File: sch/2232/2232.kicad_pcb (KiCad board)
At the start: 2 copper layers, 80 x 70 mm, 65 parts, among them J1 47346-0001, J2 IDC-06, J3 IDC-06, J4 IDC-10, J5 IDC-10, J6 6P6C, J7 Screw_Terminal_01x06, J8 Screw_Terminal_01x06, U1 FT2232D, U2 AMS1117-3.3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

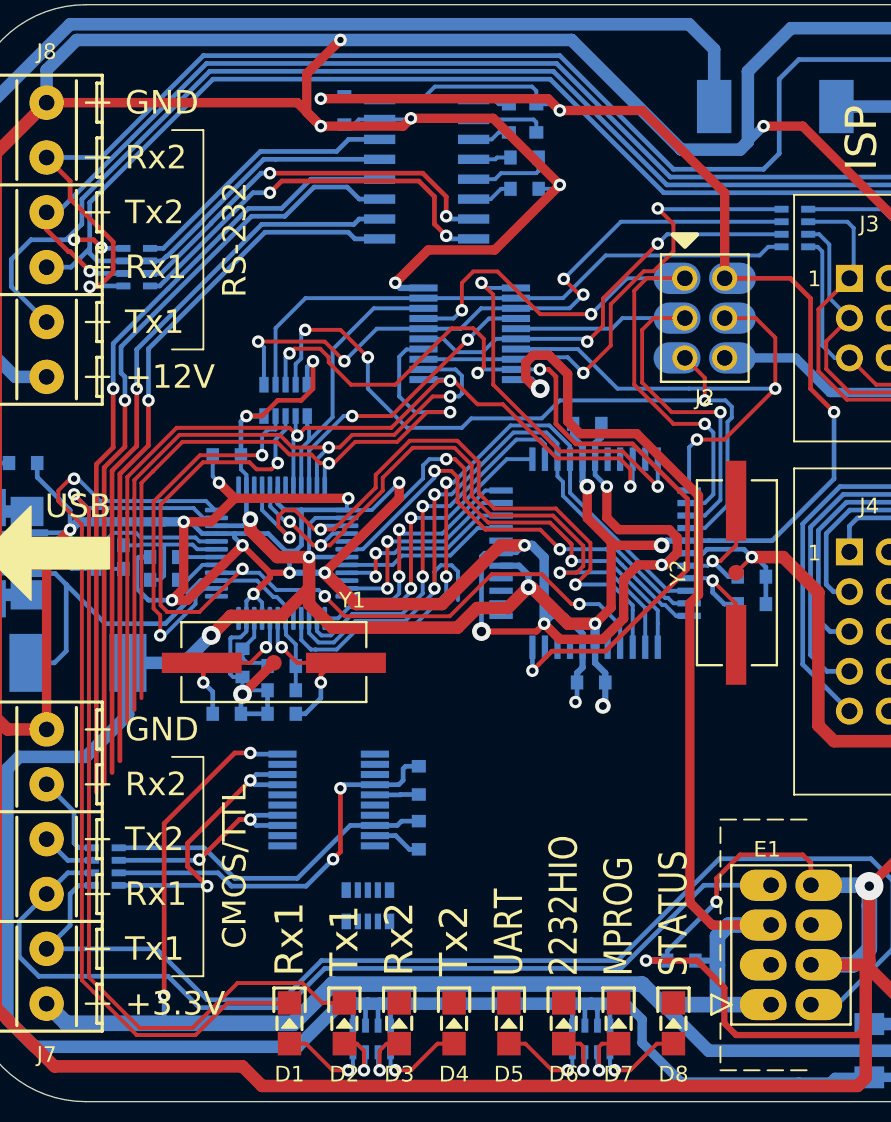
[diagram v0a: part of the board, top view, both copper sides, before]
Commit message: All footprinted elements are routed
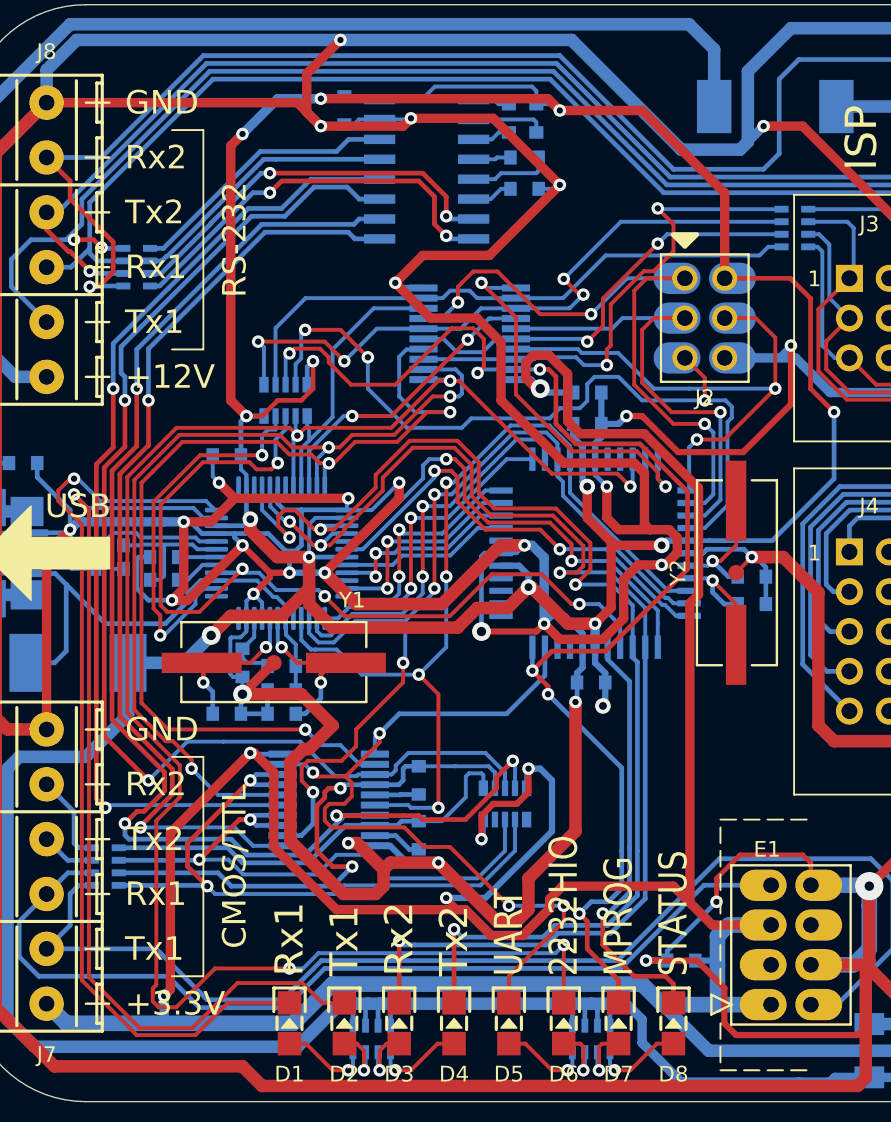
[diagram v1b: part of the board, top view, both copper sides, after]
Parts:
- added C21: 0.22u, NevaDA:C_0603, B.Cu at (99.5, 89.8)
- moved RN4 10.9 mm to (94.2, 116.0)
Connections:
- RN4 pad 1: /TX1_RS_3 -> /RX2_3V
- RN4 pad 2: /TX2_RS_3 -> /RX1_3V
- RN4 pad 3: /RX2_3V -> /TX1_RS_3
- RN4 pad 4: /RX1_3V -> /TX2_RS_3
- RN4 pad 6: /TX2_3V -> (no net)
- RN4 pad 8: (no net) -> /TX2_3V
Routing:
- net GNDD: track 725.4 -> 836.0 mm, vias 32 -> 36
- net +3V3: track 187.6 -> 251.6 mm, vias 3 -> 6
- net /EN_UART: track 0.00 -> 52.8 mm, vias 0 -> 4
- net /FBUFF: track 62.4 -> 113.4 mm, vias 3 -> 5
- net /TX2_RS_3: track 46.6 -> 88.4 mm, vias 1 -> 4
- net /LED3_~RD: track 42.9 -> 79.9 mm, vias 3 -> 4
- net /LED4_~WR: track 44.5 -> 78.2 mm, vias 3 -> 4
- net /TX1_RS_3: track 49.6 -> 77.5 mm, vias 1 -> 2
- net /MCU_LED: track 0.00 -> 27.2 mm, vias 0 -> 1
- net /MCU_BUFF: track 57.1 -> 83.8 mm, vias 4 -> 6
- net +5V: track 316.2 -> 340.9 mm, vias 13 -> 14
- net /TX2_3V: track 13.8 -> 37.6 mm
- net /TX1_3V: track 19.0 -> 42.0 mm
- net /FSCK_T1: track 46.1 -> 62.9 mm, vias 2 -> 3
- net /PAR_0_T2: track 42.6 -> 59.0 mm, vias 2 -> 4
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
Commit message: VCC routed
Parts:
- added D10: SMBJ5.0A-E3/52, NevaDA:DO-214AA_SMB, B.Cu at (126.5, 109.0)
- added Q1: BC817-40, NevaDA:SOT-23, B.Cu at (136.0, 95.0)
- added Q2: FZT1049A, NevaDA:SOT-223, B.Cu at (123.0, 93.5)
- added R11: 100, NevaDA:R_0603, B.Cu at (151.6, 78.9)
- added R12: 100, NevaDA:R_0603, B.Cu at (146.9, 78.5)
- added R13: 100, NevaDA:R_0603, B.Cu at (131.8, 94.0)
- added R8: 100, NevaDA:R_0603, B.Cu at (142.5, 78.5)
- added R9: 1 1206, NevaDA:R_1206, B.Cu at (137.0, 100.8)
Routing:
- net VCC: track 32.1 -> 196.0 mm, vias 0 -> 7
- net /IDC_VCC: track 37.2 -> 70.7 mm
- net Net-(Q1-Pad1): track 0.00 -> 22.9 mm
- net GNDD: track 836.0 -> 851.7 mm, vias 36 -> 54
- net Net-(Q1-Pad3): track 0.00 -> 11.4 mm
- net /IDC_RST: track 55.9 -> 61.6 mm
- net /IDC_MOSI: track 50.5 -> 55.3 mm
- net /IDC_MISO: track 69.4 -> 74.1 mm
- net /IDC_R: track 28.5 -> 23.8 mm
- net +5V: track 340.9 -> 336.2 mm
- net /IDC_CLK: track 63.3 -> 67.1 mm
- net /IDC_5V: track 37.4 -> 33.9 mm
- net /IDC_CS: track 33.2 -> 30.9 mm
- net /RX1_3VR: track 60.7 -> 59.6 mm, vias 0 -> 1
- net /IDC_REL: track 30.1 -> 29.6 mm

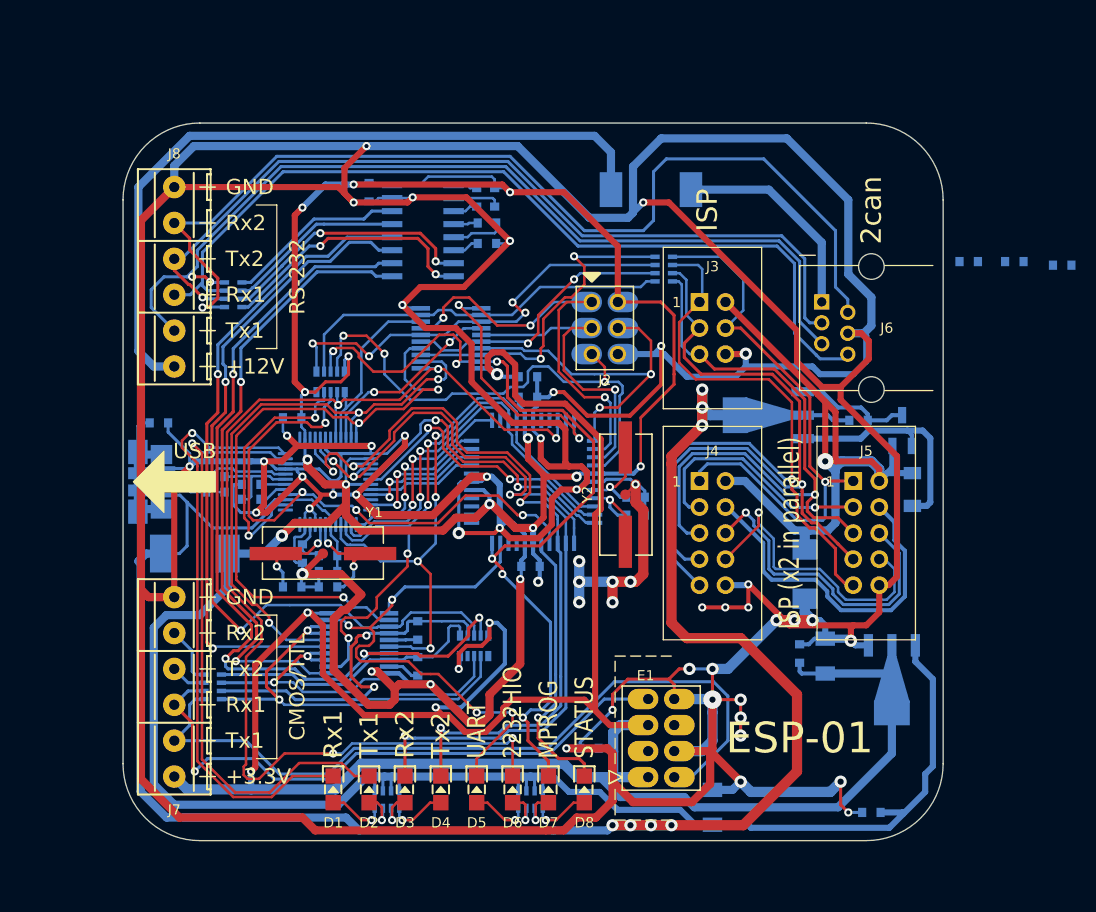
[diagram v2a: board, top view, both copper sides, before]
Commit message: IDC rotated
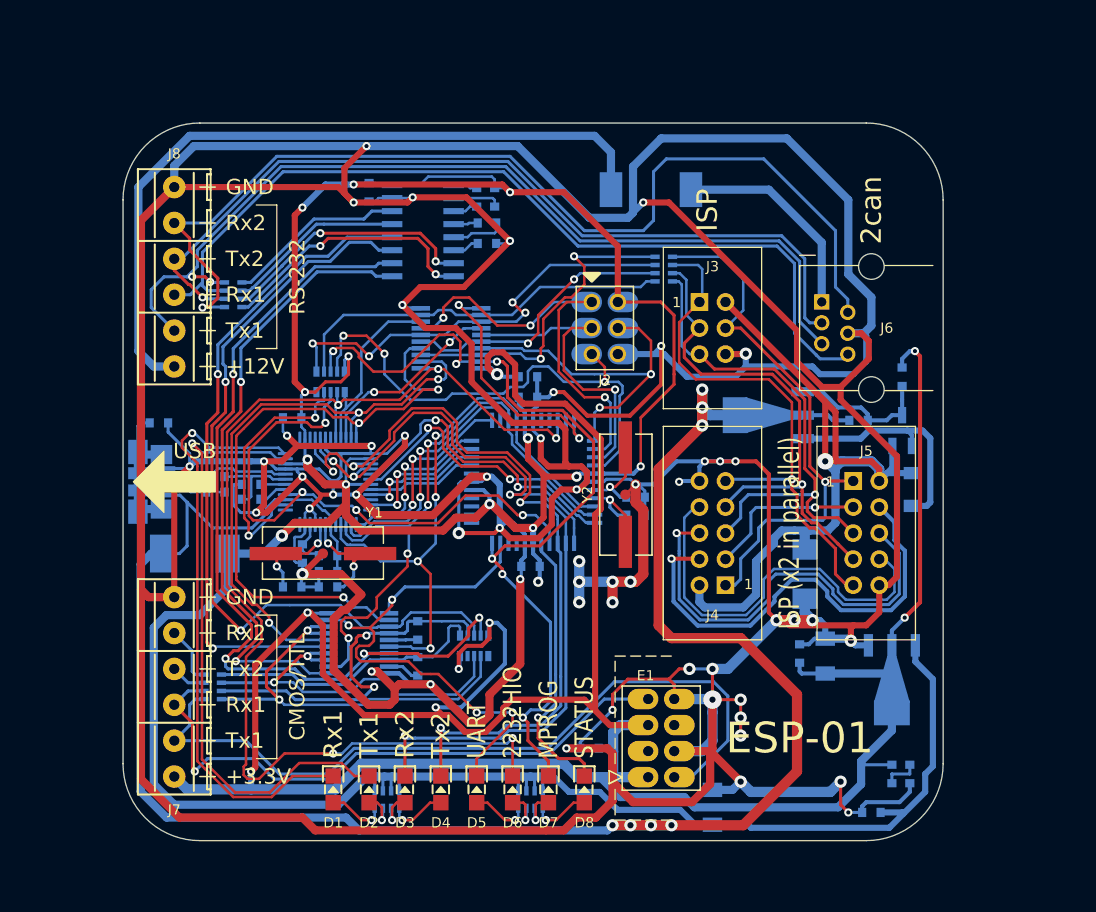
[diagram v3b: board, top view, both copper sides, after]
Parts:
- moved R11 52.3 mm to (135.0, 128.5), turned to 270 degrees
- moved R12 51.0 mm to (136.8, 128.5), turned to 270 degrees
- moved R8 13.0 mm to (136.0, 89.8), turned to 90 degrees
- turned J4 to 90 degrees
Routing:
- net +3V3: track 251.6 -> 287.2 mm, vias 6 -> 8
- net GNDD: track 851.7 -> 879.8 mm
- net /IDC_MISO: track 74.1 -> 53.3 mm
- net /IDC_CLK: track 67.1 -> 49.7 mm
- net /IDC_RST: track 61.6 -> 49.4 mm
- net /IDC_CS: track 30.9 -> 42.7 mm
- net /IDC_5V: track 33.9 -> 44.5 mm, vias 0 -> 1
- net /IDC_REL: track 29.6 -> 39.8 mm, vias 1 -> 0
- net /IDC_R: track 23.8 -> 15.8 mm
- net /IDC_VCC: track 70.7 -> 78.5 mm
- net Net-(R11-Pad2): track 0.00 -> 3.55 mm
- net Net-(Q1-Pad3): track 11.4 -> 14.3 mm
- net /IDC_MOSI: track 55.3 -> 53.8 mm
- net VCC: track 196.0 -> 197.4 mm

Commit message: No-fill zones
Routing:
- net /RX2_RSR: track 100.4 -> 101.1 mm
- net /TX1_RS_3: track 77.5 -> 76.9 mm
- added copper zone on B.Cu, net GNDD
- added copper zone on F.Cu, net GNDD

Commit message: Minor updates
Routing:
- net GNDD: track 879.8 -> 1017.6 mm, vias 54 -> 77
- net /IDC_VCC: track 78.5 -> 72.7 mm
- net +5V: track 336.2 -> 339.4 mm, vias 14 -> 15
- net /PAR_0_T2: track 59.0 -> 62.1 mm
- net /ISP_RST: track 38.4 -> 40.9 mm
- net /EEDATA: track 25.1 -> 23.0 mm
- net /IDC_REL: track 39.8 -> 38.2 mm
- net /IDC_CS: track 42.7 -> 41.1 mm
- net /FCS: track 18.2 -> 19.6 mm
- net /MCU_RST: track 50.2 -> 51.6 mm
- net /IDC_MISO: track 53.3 -> 52.2 mm
- net /USB_reset: track 57.8 -> 56.7 mm
- net /IDC_MOSI: track 53.8 -> 52.7 mm
- net /MCU_ROUT: track 24.6 -> 23.5 mm
- net /ISP_MISO: track 43.0 -> 42.2 mm
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- added copper zone on B.Cu, net +3V3

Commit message: pcb updates. Looks ready
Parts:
- moved R9 3.64 mm to (136.0, 97.2), turned to 180 degrees
- moved R13 2.92 mm to (129.2, 92.5), turned to 90 degrees
- moved R8 2.75 mm to (136.0, 87.0)
- moved Q1 2.00 mm to (136.0, 93.0)
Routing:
- net GNDD: track 1017.6 -> 1047.2 mm, vias 77 -> 84
- net /IDC_VCC: track 72.7 -> 65.5 mm
- net Net-(Q1-Pad1): track 22.9 -> 16.2 mm
- net Net-(Q1-Pad3): track 14.3 -> 17.7 mm
- net /TX2_RS_3: track 88.4 -> 86.3 mm
- net /RX2_RS_3: track 60.7 -> 58.6 mm
- net /FBUFF: track 113.4 -> 115.4 mm
- net VCC: track 197.4 -> 195.6 mm
- net /RX2_RSR: track 101.1 -> 99.4 mm
- net /EN_UART: track 52.8 -> 54.4 mm
- net +3V3: track 286.9 -> 288.4 mm
- net /ISP_RST: track 40.9 -> 39.4 mm
- net /TX1_RSR: track 90.7 -> 89.4 mm
- net /LED2: track 60.3 -> 61.6 mm
- net /TX1_RS_3: track 76.4 -> 75.2 mm
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- added copper zone on B.Cu, net VCC
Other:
- board text added: "(3)"
- board text added: "(4)"
- board text added: "(6)"
- board text added: "(8)"
- board text added: "CLK"
- board text added: "MISO"
- board text added: "MOSI"
- board text added: "RST"
- board text added: "VCC"

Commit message: PCB silk added
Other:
- board text added: "12V"
- board text added: "NOTE: TXn here is OUTPUT"
- board text added: "RX1"
- board text added: "RX2"
- board text added: "Self-prog"
- board text added: "TX1"
- board text added: "TX2"
- board text added: "WPROG version 1.0"
- board text added: "https://github.com/Nevada317/wprog"

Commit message: Gerbers exported
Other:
- board text added: "UARTs"
